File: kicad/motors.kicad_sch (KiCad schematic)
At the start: 18 parts, among them U1 DRV8848, U2 DRV8848, U3 DRV8848

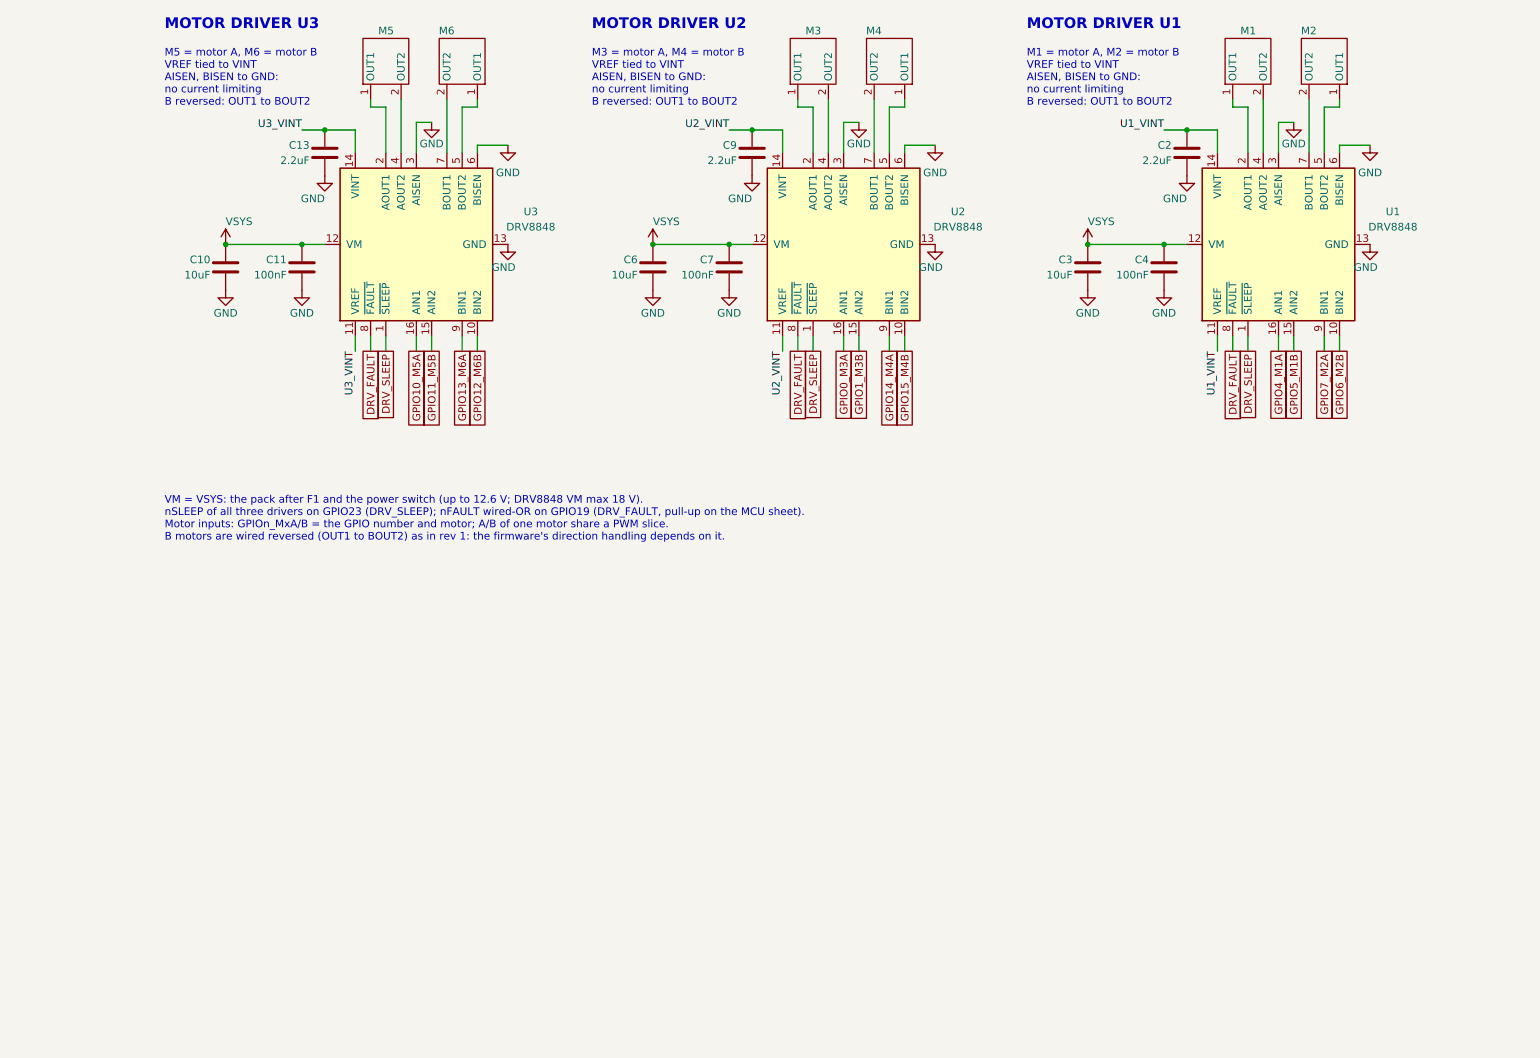
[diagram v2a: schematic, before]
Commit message: Fix the buck inductor, soft-start VSYS and limit motor current
Circuit (goosebrain.py, PARTS.md, schematic):
- L1 is a Coilcraft XAL5030-222 (Isat 9.2 A, the AP64500's max current
  limit). The old CR4030 saturated at about 3.1 A.
- VSYS soft start and clamp: C71 gate-drain and C72 gate-source on Q1,
  R40 27k, R41 10k, and an SMF14A TVS (D4) on VSYS.
- Each DRV8848 chops at about 1.33 A per bridge: 0.15 R sense resistors
  on AISEN/BISEN and a 15k/10k VREF divider from VINT, so six stalled
  motors can't reach the protector's OCD1 trip.
- U4 gets a second 10 uF (C73) and a 100 nF (C74) at VIN.
- Stock swaps after a full JLC stock check: D4 to the Littelfuse SMF14A,
  the sense resistors to YAGEO RL1206FR-7W0R15L (500 mW).

Board:
- New parts placed and routed. The sense resistors are close to their
  pins; U2's B-side runs on F.Cu only.
- 22 more VSYS vias (Q1 drain to the In3 plane, each driver's VM caps,
  both ends of U4's VIN jumper).
- C63 (AVDD) and C68 (SRP-SRN) moved next to the BQ7791501.
- Goose logo on the back silkscreen.
- Review 63: DRC 0 errors, unrouted 0, parity clean, no new DRC types.

tools/fab.py adds per-package rotation offsets read off JLC's placement
preview. The README covers them, the D4 polarity check, the corrected
current limits and the low-stock parts.

Co-Authored-By: Claude Opus 5.5 <noreply@anthropic.com>
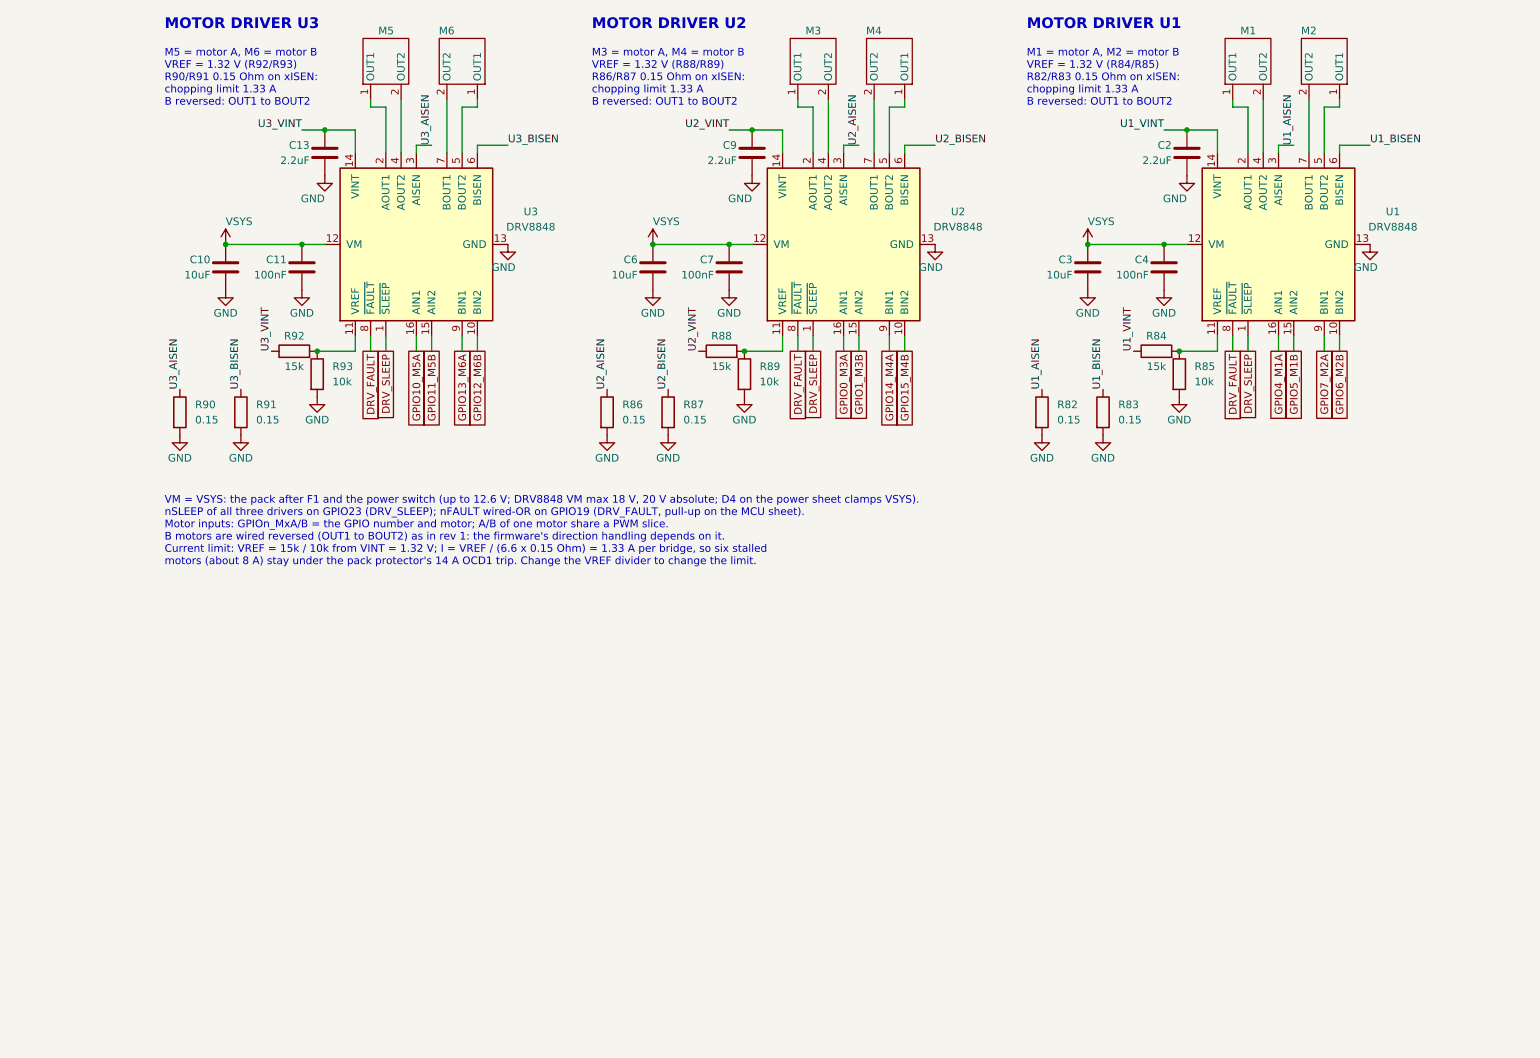
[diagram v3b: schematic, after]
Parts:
- added R82, R83, R86, R87, R90, R91: 0.15, Resistor_SMD:R_1206_3216Metric, symbol Device:R
- added R84, R88, R92: 15k, Resistor_SMD:R_0402_1005Metric, symbol Device:R
- added R85, R89, R93: 10k, Resistor_SMD:R_0402_1005Metric, symbol Device:R
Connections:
- net GND: now also R82.2, R83.2, R85.2, R86.2, R87.2, R89.2, R90.2, R91.2, R93.2; no longer U1.3 (AISEN), U1.6 (BISEN), U2.3 (AISEN), U2.6 (BISEN), U3.3 (AISEN), U3.6 (BISEN)
- net U1_VINT: now also R84.1; no longer U1.11 (VREF)
- net U2_VINT: now also R88.1; no longer U2.11 (VREF)
- net U3_VINT: now also R92.1; no longer U3.11 (VREF)
- new net: R88.2, R89.1, U2.11 (VREF)
- new net: R92.2, R93.1, U3.11 (VREF)
- new net: R84.2, R85.1, U1.11 (VREF)
- new net U1_AISEN: R82.1, U1.3 (AISEN)
- new net U1_BISEN: R83.1, U1.6 (BISEN)
- new net U2_AISEN: R86.1, U2.3 (AISEN)
- new net U2_BISEN: R87.1, U2.6 (BISEN)
- new net U3_AISEN: R90.1, U3.3 (AISEN)
- new net U3_BISEN: R91.1, U3.6 (BISEN)
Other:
- note added: "M1 = motor A, M2 = motor B VREF = 1.32 V (R84/R85) R82/R83 0.15 Ohm on xISEN: chopping limit 1.33 A B reversed: OUT1 to BOUT2"
- note added: "M3 = motor A, M4 = motor B VREF = 1.32 V (R88/R89) R86/R87 0.15 Ohm on xISEN: chopping limit 1.33 A B reversed: OUT1 to BOUT2"
- note added: "M5 = motor A, M6 = motor B VREF = 1.32 V (R92/R93) R90/R91 0.15 Ohm on xISEN: chopping limit 1.33 A B reversed: OUT1 to BOUT2"
- note added: "VM = VSYS: the pack after F1 and the power switch (up to 12.6 V; DRV8848 VM max 18 V, 20 V absolute; D4 on the power sheet clamps VSYS). nSLEEP of all three drivers on GPIO23 (DRV_SLEEP); nFAULT wired-OR on GPIO19 (DRV_FAULT, pull-up on the MCU sheet). Motor inputs: GPIOn_MxA/B = the GPIO number and motor; A/B of one motor share a PWM slice. B motors are wired reversed (OUT1 to BOUT2) as in rev 1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"
- note removed: "M1 = motor A, M2 = motor B VREF tied to VINT AISEN, BISEN to GND: no current limiting B reversed: OUT1 to BOUT2"
- note removed: "M3 = motor A, M4 = motor B VREF tied to VINT AISEN, BISEN to GND: no current limiting B reversed: OUT1 to BOUT2"
- note removed: "M5 = motor A, M6 = motor B VREF tied to VINT AISEN, BISEN to GND: no current limiting B reversed: OUT1 to BOUT2"
- note removed: "VM = VSYS: the pack after F1 and the power switch (up to 12.6 V; DRV8848 VM max 18 V). nSLEEP of all three drivers on GPIO23 (DRV_SLEEP); nFAULT wired-OR on GPIO19 (DRV_FAULT, pull-up on the MCU sheet). Motor inputs: GPIOn_MxA/B = the GPIO number and motor; A/B of one motor share a PWM slice. B motors are wired reversed (OUT1 to BOUT2) as in rev 1: the firmware's direction handling depends on it."

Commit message: Split into brain + smart pack, and support 2S packs
Brain/pack split: charging, protection and the fuse move off the brain
into a separate smart pack board (kicad-pack/goosepack), with its own
USB-C charging port. The brain drops to 4 layers, loses the charger,
PD sink, protector and SY6280, and swaps the DRV8848s for DRV8871s.

2S support on the brain:
- DRV8871 -> DRV8251A (same HSOP-8 footprint, 4.5-48 V VM). Shared VREF
  divider R107/R108/C81 from +3V3 (2.53 V) and 1.18k IPROPI resistors
  keep the 1.36 A limit.
- Q1 gate divider 27k/10k -> 47k/4.7k for -5.1 V drive at an empty 2S
  pack; C71 4.7n -> 10n to keep the ~70 us soft start.

New 2S pack variant (kicad-pack-2s/goosepack2s): BQ25798 PROG 8.2k
(2S, 750 kHz), ILIM R33 18k (~0.42 A charge), ABLIC S-8252AAH protector
in place of the BQ7791501, two HY2213-BB3A balancers with AO3400A and
47R 2512 bleed resistors, 3-pin XH balance header, R94 4.7k for trip
recovery. fab.py builds it with --board pack2s.

Several new parts still need LCSC numbers; fab.py flags each one.

Co-Authored-By: Claude Opus 5.5 <noreply@anthropic.com>
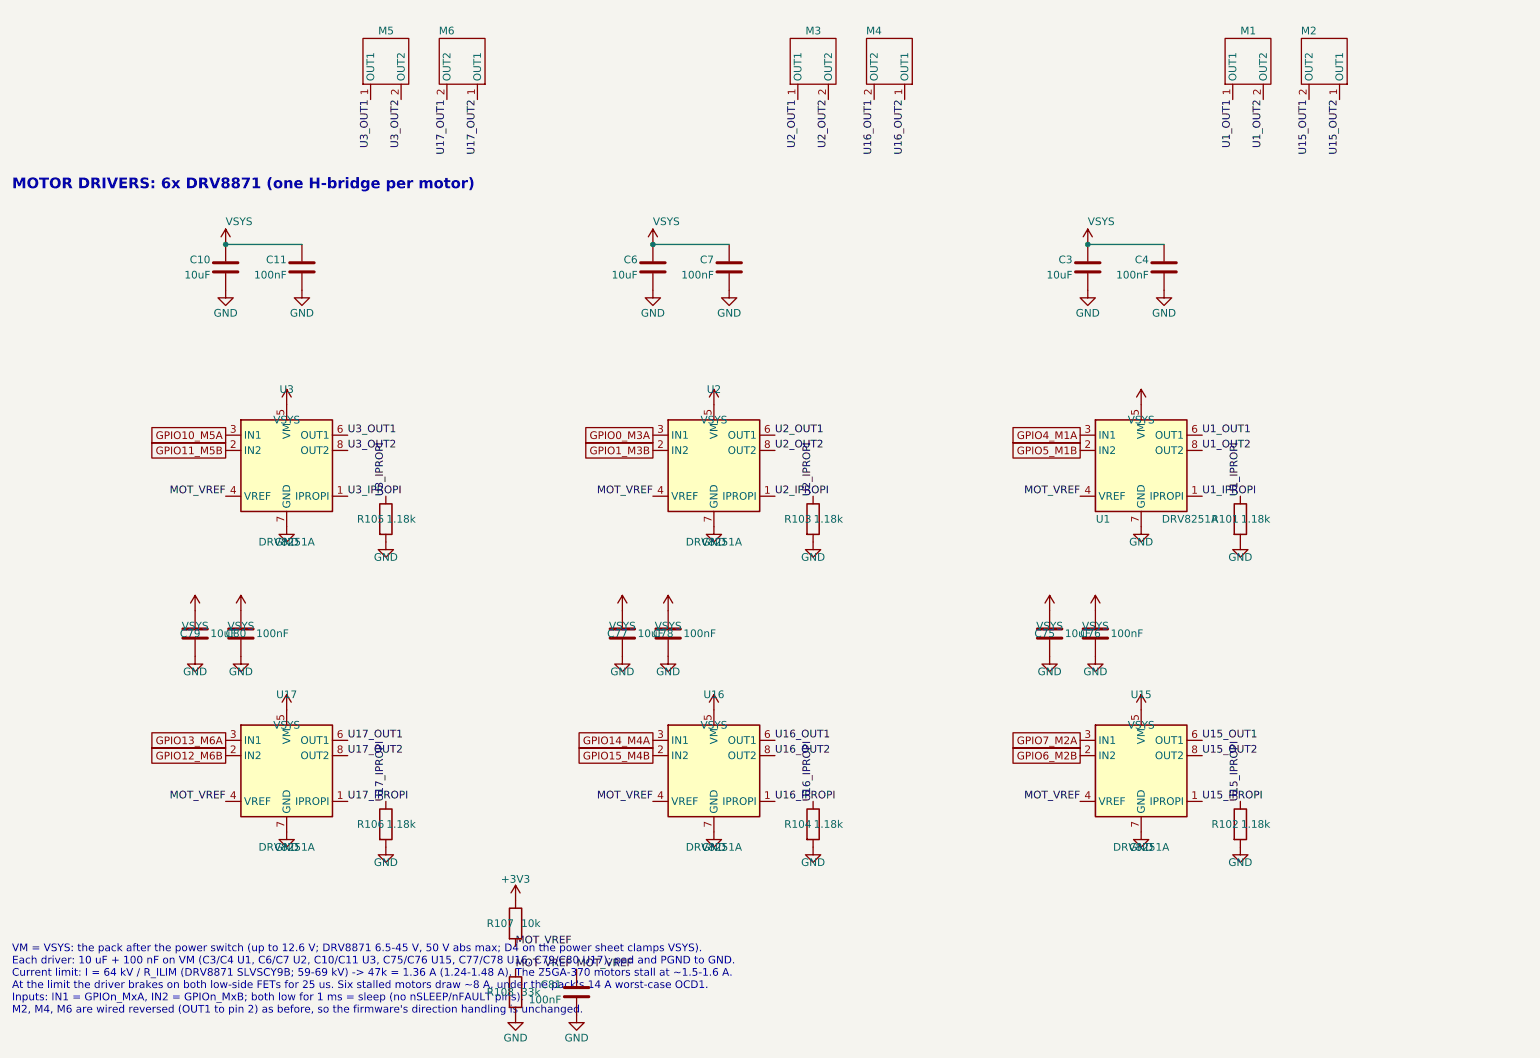
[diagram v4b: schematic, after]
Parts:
- removed C13, C2, C9: 2.2uF, Capacitor_SMD:C_0603_1608Metric, symbol Device:C
- removed R82, R83, R86, R87, R90, R91: 0.15, Resistor_SMD:R_1206_3216Metric, symbol Device:R
- removed R84, R88, R92: 15k, Resistor_SMD:R_0402_1005Metric, symbol Device:R
- removed R85, R89, R93: 10k, Resistor_SMD:R_0402_1005Metric, symbol Device:R
- removed U1, U2, U3: DRV8848, Package_SO:TSSOP-16-1EP_4.4x5mm_P0.65mm, symbol Driver_Motor:DRV8848
- added C75, C77, C79: 10uF, Capacitor_SMD:C_0805_2012Metric, symbol Device:C
- added C76, C78, C80: 100nF, Capacitor_SMD:C_0805_2012Metric, symbol Device:C
- added C81: 100nF, Capacitor_SMD:C_0402_1005Metric, symbol Device:C
- added R101, R102, R103, R104, R105, R106: 1.18k, Resistor_SMD:R_0402_1005Metric, symbol Device:R
- added R107: 10k, Resistor_SMD:R_0402_1005Metric, symbol Device:R
- added R108: 33k, Resistor_SMD:R_0402_1005Metric, symbol Device:R
- added U1, U15, U16, U17, U2, U3: DRV8251A, Package_SO:Texas_HTSOP-8-1EP_3.9x4.9mm_P1.27mm_EP2.95x4.9mm_Mask2.4x3.1mm_ThermalVias, symbol hexyhustle:DRV8251ADDA
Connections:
- net GND: now also C75.2, C76.2, C77.2, C78.2, C79.2, C80.2, C81.2, R101.2, R102.2, R103.2, R104.2, R105.2, R106.2, R108.2, U1.7 (GND), U1.9 (GND), U15.7 (GND), U15.9 (GND), U16.7 (GND), U16.9 (GND), U17.7 (GND), U17.9 (GND), U2.7 (GND), U2.9 (GND), U3.7 (GND), U3.9 (GND)
- net GPIO0_M3A: now also U2.3 (IN1)
- net GPIO10_M5A: now also U3.3 (IN1)
- net GPIO11_M5B: now also U3.2 (IN2)
- net GPIO12_M6B: now also U17.2 (IN2)
- net GPIO13_M6A: now also U17.3 (IN1)
- net GPIO14_M4A: now also U16.3 (IN1)
- net GPIO15_M4B: now also U16.2 (IN2)
- net GPIO1_M3B: now also U2.2 (IN2)
- net GPIO4_M1A: now also U1.3 (IN1)
- net GPIO5_M1B: now also U1.2 (IN2)
- net GPIO6_M2B: now also U15.2 (IN2)
- net GPIO7_M2A: now also U15.3 (IN1)
- net VSYS: now also C75.1, C76.1, C77.1, C78.1, C79.1, C80.1, U1.5 (VM), U15.5 (VM), U16.5 (VM), U17.5 (VM), U2.5 (VM), U3.5 (VM)
- net U2_OUT1: now reaches M3.1 (OUT1)
- net U2_OUT1: now also U2.6 (OUT1)
- net U2_OUT2: now reaches M3.2 (OUT2)
- net U2_OUT2: now also U2.8 (OUT2)
- net U3_OUT1: now reaches M5.1 (OUT1)
- net U3_OUT1: now also U3.6 (OUT1)
- net U3_OUT2: now reaches M5.2 (OUT2)
- net U3_OUT2: now also U3.8 (OUT2)
- net U17_OUT2: now reaches M6.1 (OUT1)
- net U17_OUT2: now also U17.8 (OUT2)
- net U17_OUT1: now reaches M6.2 (OUT2)
- net U17_OUT1: now also U17.6 (OUT1)
- net U15_OUT2: now reaches M2.1 (OUT1)
- net U15_OUT2: now also U15.8 (OUT2)
- net U15_OUT1: now reaches M2.2 (OUT2)
- net U15_OUT1: now also U15.6 (OUT1)
- net U16_OUT2: now reaches M4.1 (OUT1)
- net U16_OUT2: now also U16.8 (OUT2)
- net U16_OUT1: now reaches M4.2 (OUT2)
- net U16_OUT1: now also U16.6 (OUT1)
- net U1_OUT1: now reaches M1.1 (OUT1)
- net U1_OUT1: now also U1.6 (OUT1)
- net U1_OUT2: now reaches M1.2 (OUT2)
- net U1_OUT2: now also U1.8 (OUT2)
- new net +3V3: R107.1
- new net MOT_VREF: C81.1, R107.2, R108.1, U1.4 (VREF), U15.4 (VREF), U16.4 (VREF), U17.4 (VREF), U2.4 (VREF), U3.4 (VREF)
- new net U15_IPROPI: R102.1, U15.1 (IPROPI)
- new net U16_IPROPI: R104.1, U16.1 (IPROPI)
- new net U17_IPROPI: R106.1, U17.1 (IPROPI)
- new net U1_IPROPI: R101.1, U1.1 (IPROPI)
- new net U2_IPROPI: R103.1, U2.1 (IPROPI)
- new net U3_IPROPI: R105.1, U3.1 (IPROPI)
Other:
- note added: "MOTOR DRIVERS: 6x DRV8871 (one H-bridge per motor)"
- note added: "VM = VSYS: the pack after the power switch (up to 12.6 V; DRV8871 6.5-45 V, 50 V abs max; D4 on the power sheet clamps VSYS). Each driver: 10 uF + 100 nF on VM (C3/C4 U1, C6/C7 U2, C10/C11 U3, C75/C76 U15, C77/C78 U16, C79/C80 U17); pad and PGND to GND. Current limit: I = 64 kV / R_ILIM (DRV8871 SLVSCY9B; 59-69 kV) -> 47k = 1.36 A (1.24-1.48 A). The 25GA-370 motors stall at ~1.5-1.6 A. At the lim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"
- note removed: "M1 = motor A, M2 = motor B VREF = 1.32 V (R84/R85) R82/R83 0.15 Ohm on xISEN: chopping limit 1.33 A B reversed: OUT1 to BOUT2"
- note removed: "M3 = motor A, M4 = motor B VREF = 1.32 V (R88/R89) R86/R87 0.15 Ohm on xISEN: chopping limit 1.33 A B reversed: OUT1 to BOUT2"
- note removed: "M5 = motor A, M6 = motor B VREF = 1.32 V (R92/R93) R90/R91 0.15 Ohm on xISEN: chopping limit 1.33 A B reversed: OUT1 to BOUT2"
- note removed: "MOTOR DRIVER U1"
- note removed: "MOTOR DRIVER U2"
- note removed: "MOTOR DRIVER U3"
- note removed: "VM = VSYS: the pack after F1 and the power switch (up to 12.6 V; DRV8848 VM max 18 V, 20 V absolute; D4 on the power sheet clamps VSYS). nSLEEP of all three drivers on GPIO23 (DRV_SLEEP); nFAULT wired-OR on GPIO19 (DRV_FAULT, pull-up on the MCU sheet). Motor inputs: GPIOn_MxA/B = the GPIO number and motor; A/B of one motor share a PWM slice. B motors are wired reversed (OUT1 to BOUT2) as in rev 1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"
